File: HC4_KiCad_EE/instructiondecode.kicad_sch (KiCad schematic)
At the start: 28 parts, among them IC11 74HC02, IC12 74HC00, IC13 74HC4053, IC14 74HC74

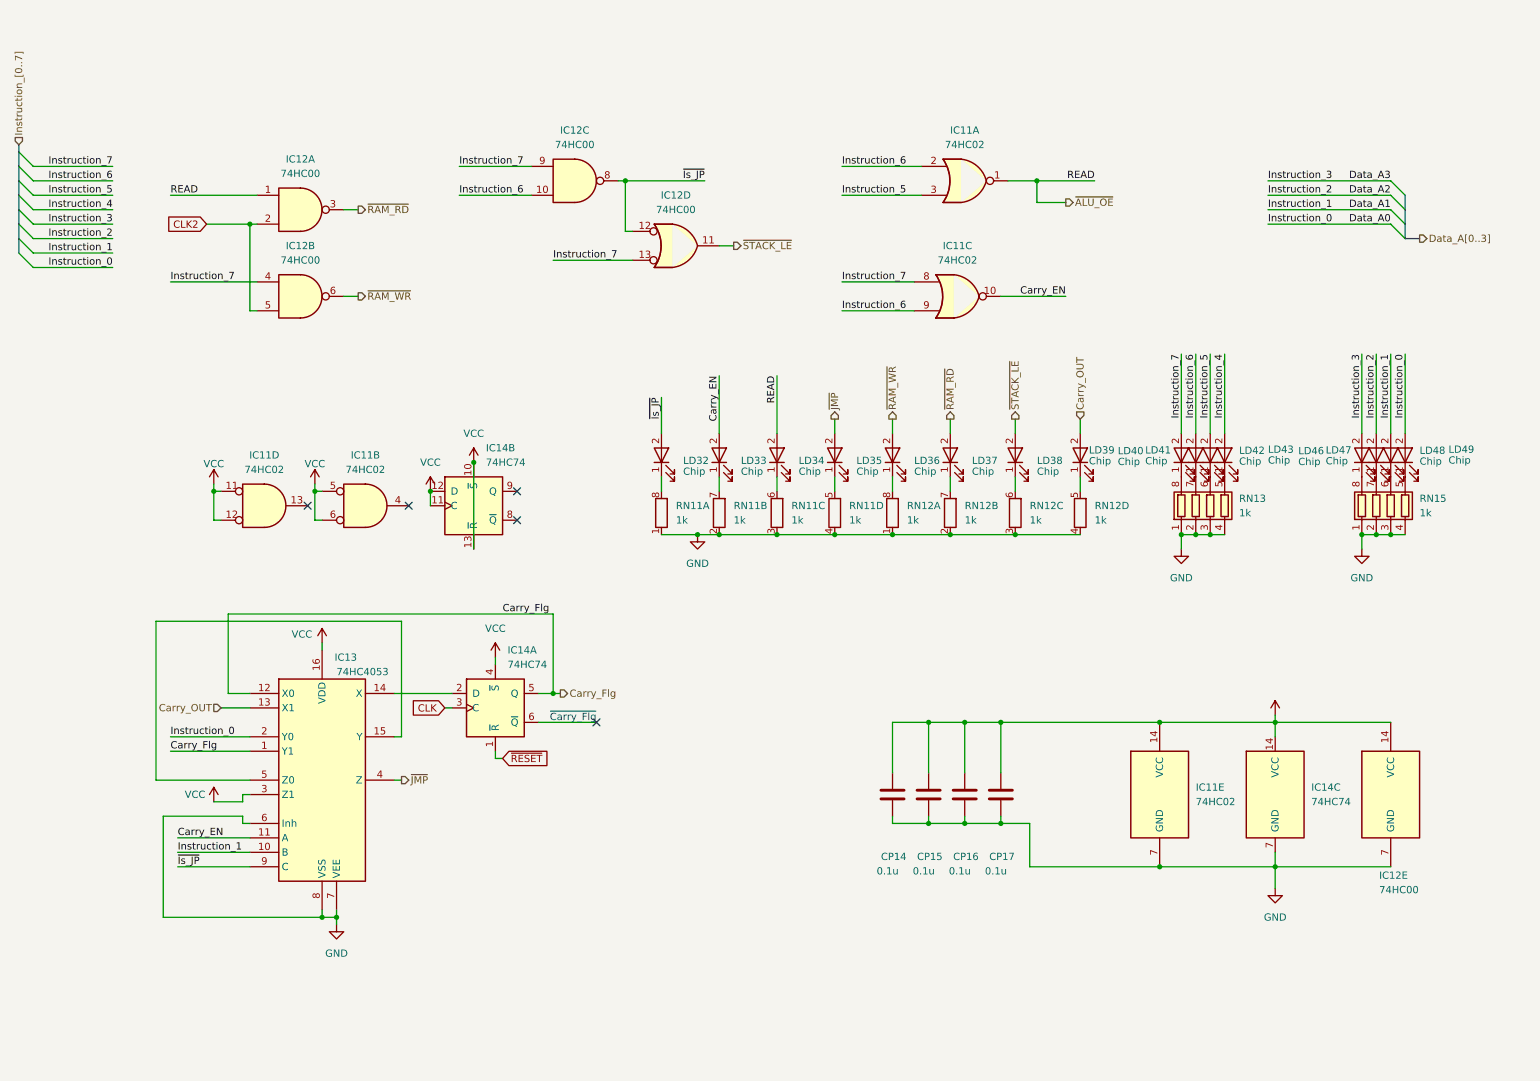
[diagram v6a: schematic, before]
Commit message: 配線進捗、7474を使った変な回路
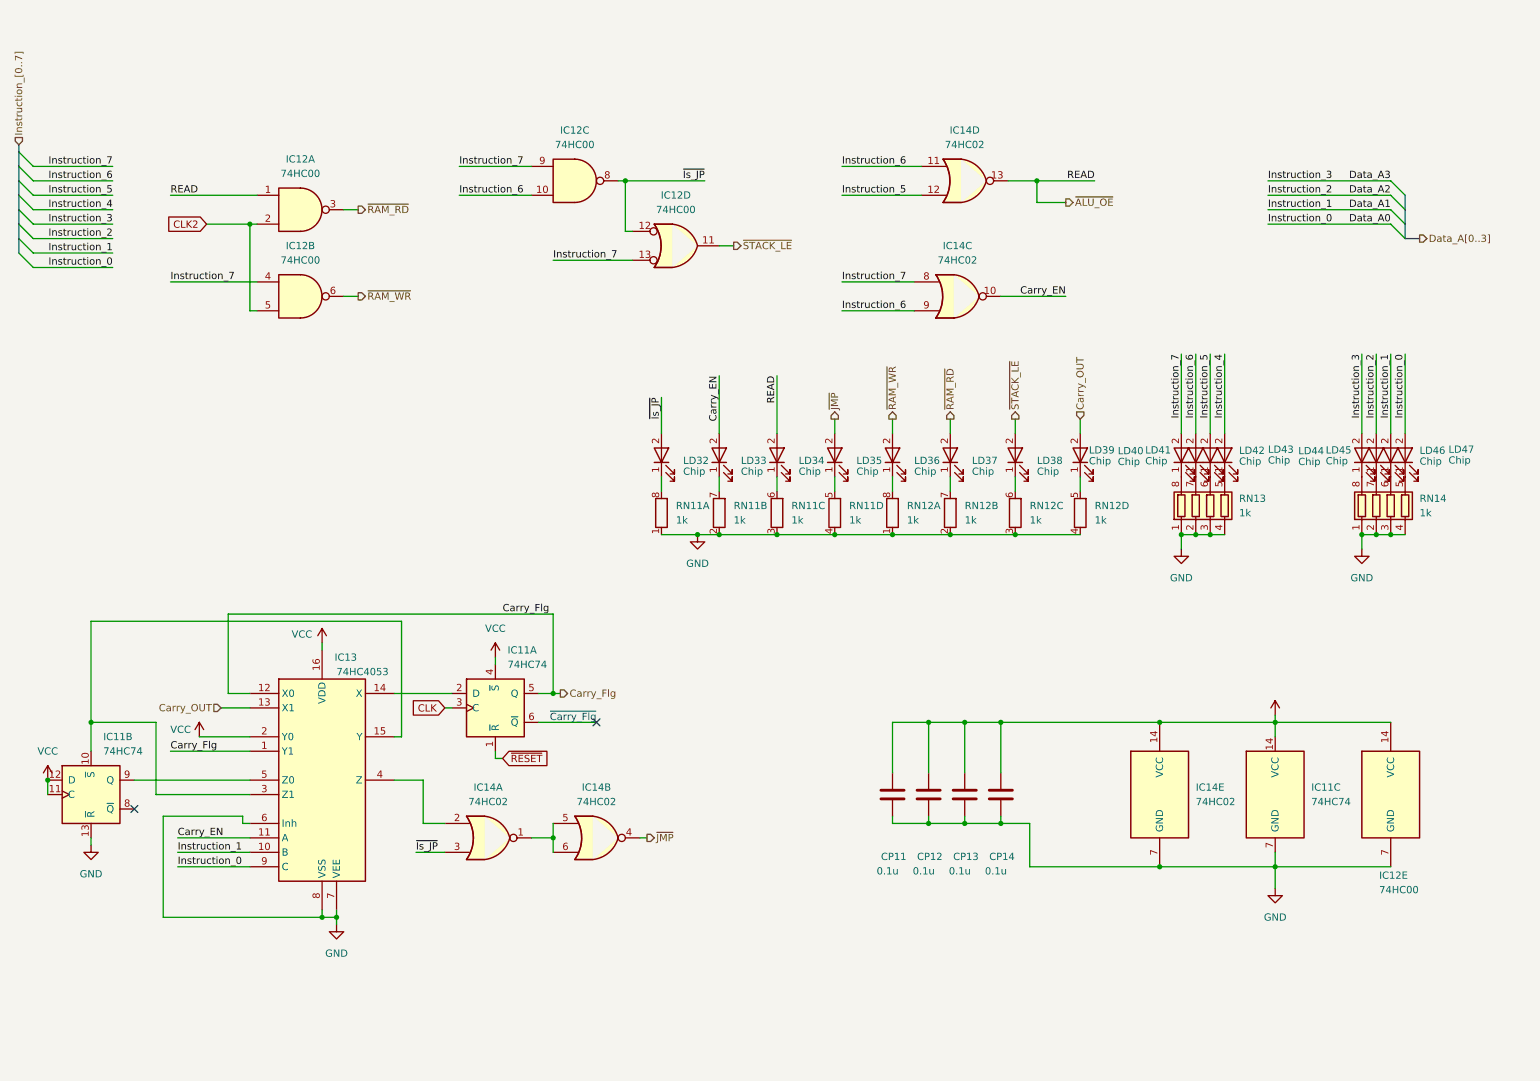
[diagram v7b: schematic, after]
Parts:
- removed unit 4 of IC11
- removed unit 2 of IC11
- removed unit 2 of IC14
- added unit 2 of IC11
- added unit 2 of IC14
- added unit 4 of IC14
- renumbered CP14 to CP11, CP15 to CP12, CP16 to CP13, CP17 to CP14, IC14 to IC11, IC11 to IC14, LD46 to LD44, LD47 to LD45, LD48 to LD46, LD49 to LD47, RN15 to RN14
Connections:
- net Data_A0: now also IC13.9 (C); no longer IC13.2 (Y0)
- net GND: now also IC11.13 (~{R})
- net Instruction_5: now also IC14.12; no longer IC14.3
- net Instruction_6: now also IC14.11; no longer IC14.2
- net VCC: now also IC13.2 (Y0), IC11.11 (C), IC11.12 (D); no longer IC13.3 (Z1)
- net ~{ALU_OE}: now also IC14.13; no longer IC14.1
- net ~{Is_JP}: now also IC14.3; no longer IC13.9 (C)
- net ~{JMP}: now also IC14.4; no longer IC13.4 (Z)
- net at IC13.15 (Y): now also IC13.3 (Z1), IC11.10 (~{S}); no longer IC13.5 (Z0)
- new net: IC14.1, IC14.5, IC14.6
- new net: IC11.9 (Q), IC13.5 (Z0)
- new net: IC13.4 (Z), IC14.2
- no-connect marks 5 -> 2
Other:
- moved on the sheet: IC14A

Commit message: もち
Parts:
- removed LD44, LD45: Chip, LED_SMD:LED_0603_1608Metric, symbol Device2:LED_
- renumbered LD38 to LD36, LD36 to LD38, LD46 to LD44, LD47 to LD45
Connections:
- net GND: no longer RN12.1 (R1.1), RN12.2 (R2.1), RN12.3 (R3.1)
- net VCC: now also RN12.1 (R1.1), RN12.2 (R2.1), RN12.3 (R3.1)
- net ~{RAM_RD}: now also LD37.1 (K); no longer LD37.2
- net ~{RAM_WR}: now also LD38.1 (K); no longer LD38.2
- net ~{STACK_LE}: now also LD36.1 (K); no longer LD36.2
- net at LD33.1 (K): now also RN11.6 (R3.2); no longer RN11.7 (R2.2)
- net at RN12.8 (R1.2): now also LD38.2; no longer LD38.1 (K)
- net at RN12.7 (R2.2): now also LD37.2; no longer LD37.1 (K)
- net at LD32.1 (K): now also RN11.5 (R4.2); no longer RN11.8 (R1.2)
- net at LD35.1 (K): now also RN11.8 (R1.2); no longer RN11.5 (R4.2)
- net at LD34.1 (K): now also RN11.7 (R2.2); no longer RN11.6 (R3.2)
- net at RN12.6 (R3.2): now also LD36.2; no longer LD36.1 (K)
- no-connect marks 2 -> 4
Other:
- moved on the sheet: LD36, LD37, LD38, RN11A, RN11B, RN11C, RN11D, RN12A, RN12B, RN12C
